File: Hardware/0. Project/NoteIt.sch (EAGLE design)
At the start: 61 parts, among them CN1 USB 3.2 Gen 2 Type C Receptac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, CN3 Micro-SD Card, CN4 FTSH-105-01-L-DV-K-TR, CN6 Lithium Ion Polymer, IC2 MCP73831/OT, IC5 S-8261ACMMD-G4MT2U, Q1 SI2374DS, Q2 SI2374DS, Q4 BC817-16LT1SMD, SW1 KY-040, U1 SN74AHC1G125DBV, U10 MSP430FR2476TPTR, U2 GL823K, U3 TLV75530PDBVR, U4 TS3A27518EPWR, U8 DS3231/SO, X2 CRYSTAL-MINI

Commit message: board design wip
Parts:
- removed CN2: (no value), con-ptr500:AK500/2-H
- added P1: OSTTE020104, Terminal Block 2P 3.5pitch:OSTTE020104
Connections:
- net 0V: now also P1.2; no longer CN2-2.KL
- net N$4: now also P1.1; no longer CN2-1.KL
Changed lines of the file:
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@@
 <setting verticaltext="up"/>
 </settings>
-<grid distance="0.025" unitdist="inch" unit="inch" style="lines" multiple="1" display="no" altdistance="0.01" altunitdist="inch" altunit="inch"/>
+<grid distance="0.1" unitdist="inch" unit="inch" style="lines" multiple="1" display="no" altdistance="0.01" altunitdist="inch" altunit="inch"/>
 <layers>
 <layer number="1" name="Top" color="4" fill="1" visible="no" active="no"/>
@@
 <part name="SUPPLY28" library="My-Supply" deviceset="0V" device=""/>
 <part name="SUPPLY29" library="My-Supply" deviceset="3.3V" device=""/>
-<part name="CN2" library="con-ptr500" deviceset="AK500/2-H" device="" package3d_urn="urn:adsk.eagle:package:9901/1" override_package3d_urn="urn:adsk.eagle:package:32815263/2" override_package_urn="urn:adsk.eagle:footprint:9865/1"/>
 <part name="SUPPLY32" library="My-Supply" deviceset="0V" device=""/>
 <part name="R1" library="My-RLC" deviceset="R_" device="0603" package3d_urn="urn:adsk.eagle:package:23494030/2"/>
@@
 <part name="SUPPLY12" library="My-Supply" deviceset="0V" device=""/>
 <part name="CN3" library="Micro SD" deviceset="MICROSD-PUSH-OUT" device="" package3d_urn="urn:adsk.eagle:package:32766245/3" value="Micro-SD Card"/>
-<part name="BAT1" library="SamacSys_Parts" deviceset="CR1220" device=""/>
+<part name="BAT1" library="SamacSys_Parts" deviceset="CR1220" device="" package3d_urn="urn:adsk.eagle:package:32858608/4"/>
 <part name="CN6" library="Battery" deviceset="BATTERY" device="JST-2" package3d_urn="urn:adsk.eagle:package:32835973/2" value="Lithium Ion Polymer"/>
 <part name="Q1" library="SI2374DS" deviceset="SI2374DS" device="SOT23" package3d_urn="urn:adsk.eagle:package:32844852/2" value="SI2374DS"/>
 <part name="Q2" library="SI2374DS" deviceset="SI2374DS" device="SOT23" package3d_urn="urn:adsk.eagle:package:32844852/2" value="SI2374DS"/>
 <part name="U3" library="TLV75530PDBVR" deviceset="TLV75530PDBVR" device="" package3d_urn="urn:adsk.eagle:package:32842001/2"/>
+<part name="P1" library="Terminal Block 2P 3.5pitch" deviceset="OSTTE020104" device="" override_package3d_urn="urn:adsk.eagle:package:32867978/2" override_package_urn="urn:adsk.eagle:footprint:32867979/1"/>
 </parts>
 <sheets>
@@
 <attribute name="VALUE" x="288.3154" y="76.2" size="1.778" layer="96" align="center"/>
 </instance>
-<instance part="CN2" gate="-1" x="273.685" y="57.15" smashed="yes" grouprefs="DATALOGGER_INPUT">
-<attribute name="NAME" x="272.415" y="58.039" size="1.778" layer="95" rot="R180"/>
-</instance>
-<instance part="CN2" gate="-2" x="273.685" y="43.18" smashed="yes" grouprefs="DATALOGGER_INPUT">
-<attribute name="NAME" x="272.415" y="44.069" size="1.778" layer="95" rot="R180"/>
-<attribute name="VALUE" x="269.875" y="39.497" size="1.778" layer="96"/>
-</instance>
 <instance part="SUPPLY32" gate="G$1" x="55.245" y="153.67" smashed="yes" grouprefs="MICRO_SDCARD_CONTROLLER"/>
 <instance part="R1" gate="G$1" x="55.245" y="191.77" smashed="yes" rot="R270" grouprefs="MICRO_SDCARD_CONTROLLER">
@@
 <attribute name="NAME" x="320.04" y="387.715" size="2.0828" layer="95" ratio="10" rot="SR0"/>
 <attribute name="VALUE" x="320.04" y="385.255" size="2.0828" layer="96" ratio="10" rot="SR0"/>
+</instance>
+<instance part="P1" gate="G$1" x="273.685" y="57.15" smashed="yes" rot="MR0" grouprefs="DATALOGGER_INPUT">
+<attribute name="NAME" x="273.685" y="59.69271875" size="1.271359375" layer="95" rot="MR0"/>
+<attribute name="VALUE" x="271.137209375" y="39.37" size="1.271559375" layer="96" rot="MR90"/>
 </instance>
 </instances>
@@
 <wire x1="288.29" y1="49.53" x2="288.29" y2="43.18" width="0.1524" layer="91" grouprefs="DATALOGGER_INPUT"/>
 <junction x="288.29" y="43.18" grouprefs="DATALOGGER_INPUT"/>
-<pinref part="CN2" gate="-2" pin="KL"/>
 <pinref part="SUPPLY28" gate="G$1" pin="0V"/>
 <wire x1="288.29" y1="38.735" x2="288.29" y2="43.18" width="0.1524" layer="91" grouprefs="DATALOGGER_INPUT"/>
+<pinref part="P1" gate="G$1" pin="2"/>
+<wire x1="278.765" y1="54.61" x2="278.765" y2="43.18" width="0.1524" layer="91"/>
 </segment>
 <segment>
@@
 <pinref part="U1" gate="G$1" pin="IN"/>
 <wire x1="278.765" y1="57.15" x2="280.67" y2="57.15" width="0.1524" layer="91" grouprefs="DATALOGGER_INPUT"/>
-<pinref part="CN2" gate="-1" pin="KL"/>
-</segment>
-</net>
+<pinref part="P1" gate="G$1" pin="1"/>
+</segment>
+</net>

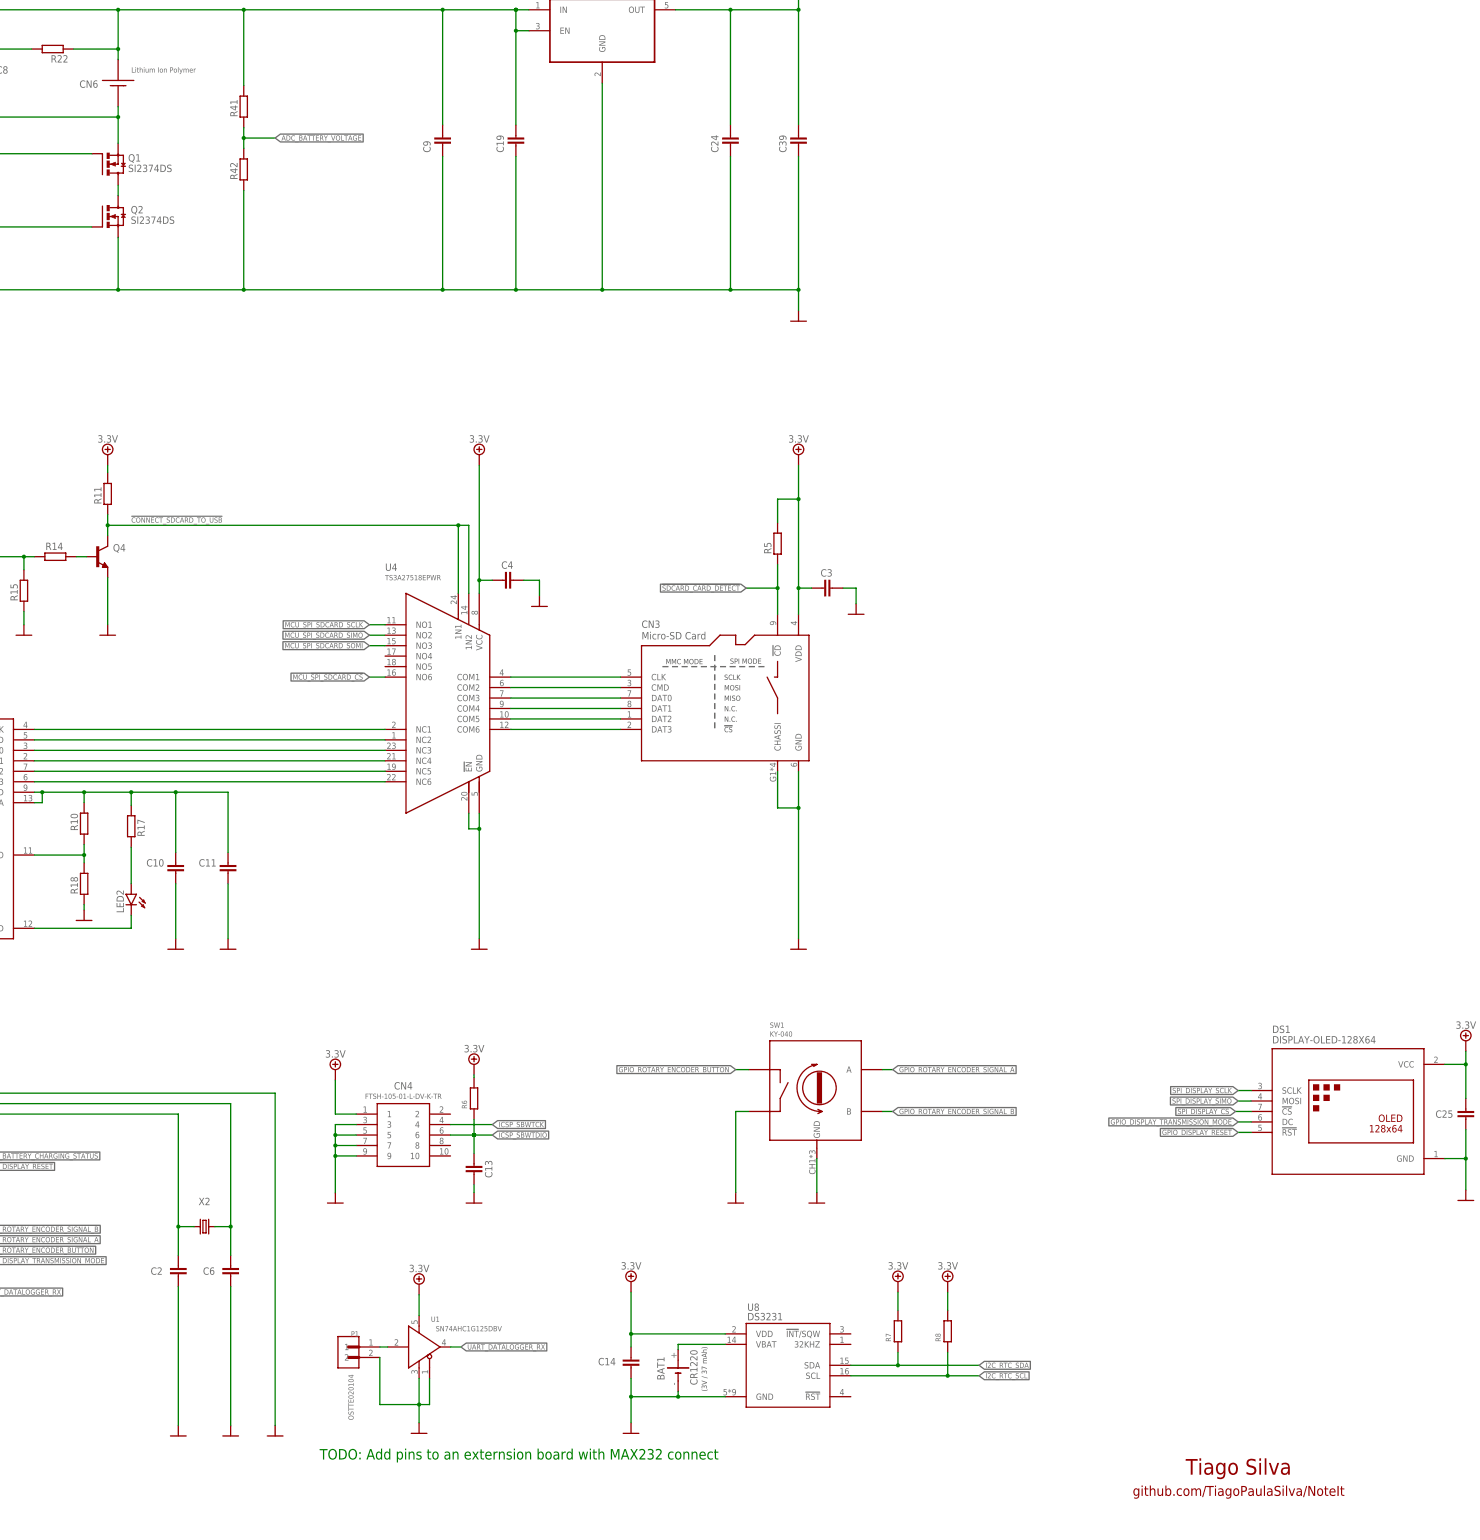
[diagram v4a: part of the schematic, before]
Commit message: Added external pull ups to rotary encoder
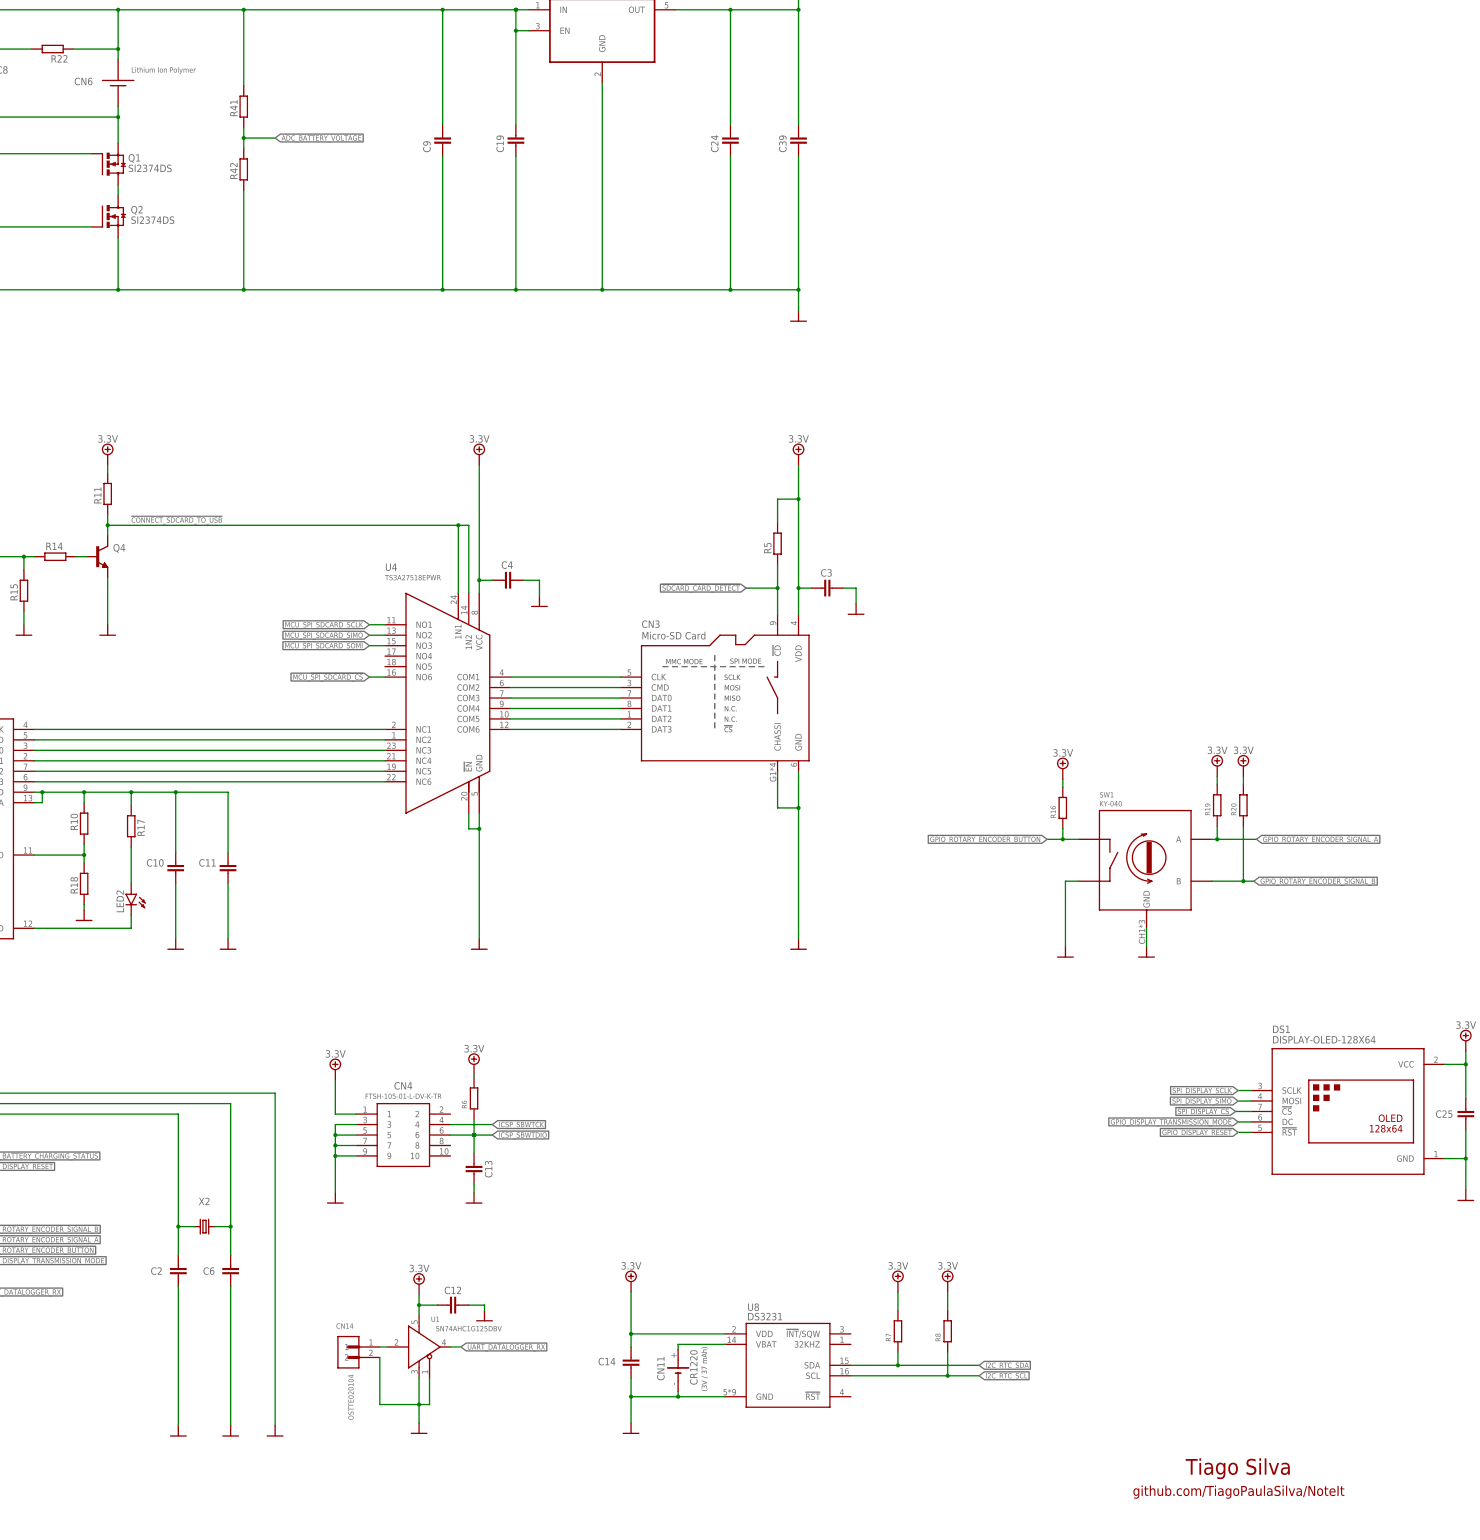
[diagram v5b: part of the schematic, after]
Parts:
- added C12: (no value), My-RLC:C_0603
- added R16, R19, R20: (no value), My-RLC:R_0603
- renumbered BAT1 to CN11, P1 to CN14
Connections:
- net 0V: now also C12.2
- net 3.3V: now also C12.1, R16.1, R19.1, R20.1
- net GPIO_ROTARY_ENCODER_BUTTON: now also R16.2
- net GPIO_ROTARY_ENCODER_SIGNAL_A: now also R19.2
- net GPIO_ROTARY_ENCODER_SIGNAL_B: now also R20.2
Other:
- note removed: "TODO: Add pins to an externsion board with MAX232 connect"
- moved on the sheet: SW1

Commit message: NoteIt v1.0 release
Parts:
- removed C25, C39: (no value), My-RLC:C_0603
- removed CN11: CR1220, SamacSys_Parts:CR1220
- removed CN14: OSTTE020104, Terminal Block 2P 3.5pitch:OSTTE020104
- removed IC2: MCP73831/OT, adafruit:MCP73831/OT
- removed IC5: S-8261ACMMD-G4MT2U, SamacSys_Parts:S-8261ACMMD-G4MT2U
- removed Q4: BC817-16LT1SMD, transistor-npn:BC817-16LT1SMD
- removed R41, R42: (no value), My-RLC:R_0603
- removed U10: MSP430FR2476TPTR, MSP430FR2476TPTR:MSP430FR2476TPTR
- removed X2: CRYSTAL-MINI, crystal-geyer_V1_0:CRYSTAL-MINI
- added C17, C20: 100nF, My-RLC:C_0603
- added CN2: Lithium Ion Polymer, Battery:BATTERYJST-2
- added CN5: CR1220, SamacSys_Parts:CR1220
- added Q3: SI2374DS, SI2374DS:SI2374DSSOT23
- added R21, R23: 10k (5%), My-RLC:R_0603
- added U5: SN74AHC1G125DBV, SN74AHC1G125DRLR:SN74AHC1G125DBV
- added U6: TS3A27518EPWR, TS3A27518EPWR:TS3A27518EPWR
- added U7: TLV75530PDBVR, TLV75530PDBVR:TLV75530PDBVR
- added Y1: 32.768 kHz, crystal-geyer_V1_0:CRYSTAL-MINI
- C1: value (none) -> 10uF x 10V; PN (none) -> GRM188R61A106ME69D
- C10: value (none) -> 10uF
- C11, C12, C15, C16, C19, C4, C7: value (none) -> 100nF
- C13: value (none) -> 1nF x 50V
- C14, C18: value (none) -> 1uF
- C2: value (none) -> 100nF; PN C0603C220J1GACTU -> C0603C104M5RACTU
- C21: value (none) -> 100nF; PN GRM188R61A106ME69D -> (none)
- C3: value (none) -> 4.7nF
- C5: value (none) -> 10uF; PN C0603C104M5RACTU -> (none)
- C6: value (none) -> 100nF; PN C0603C220J1GACTU -> (none)
- C8, C9: value (none) -> 22pF x 100V; PN (none) -> C0603C220J1GACTU
- CN3: value Micro-SD Card -> OSTTE020104; device Micro SD:MICROSD-PUSH-OUT -> Terminal Block 2P 3.5pitch:OSTTE020104
- CN6: value Lithium Ion Polymer -> Micro-SD Card; device Battery:BATTERYJST-2 -> Micro SD:MICROSD-PUSH-OUT
- Q1: value SI2374DS -> BC817; device SI2374DS:SI2374DSSOT23 -> transistor-npn:BC817-16LT1SMD
- R1, R15, R2, R4: value (none) -> 1M
- R10, R19, R20: value (none) -> 4K7 (5%)
- R11: value (none) -> 4k7
- R12: value (none) -> 10k
- R13, R18: value (none) -> 10k (5%)
- R14: value (none) -> 1k (5%)
- R16: value (none) -> 1M; PN RC0603JR-1047KL -> (none)
- R17: value (none) -> 47k (5%); PN (none) -> RC0603JR-1047KL
- R22: value (none) -> 10k (5%); PN (none) -> RC0603JR-1047KL
- R3: value (none) -> 5k1 (5%)
- R5: value (none) -> 4K7
- R6: value (none) -> 5k1 (5%); PN RC0603JR-1047KL -> (none)
- R7: value (none) -> 2k; PN RC0603JR-1047KL -> (none)
- R8: value (none) -> 10k (5%); PN RC0603JR-1047KL -> (none)
- R9: value (none) -> 470R
- U1: value SN74AHC1G125DBV -> MCP73831/2; device SN74AHC1G125DRLR:SN74AHC1G125DBV -> adafruit:MCP73831/OT
- U2: value GL823K -> MSP430FR2476TPTR; device SamacSys_Parts:GL823K -> MSP430FR2476TPTR:MSP430FR2476TPTR; PN (none) -> MSP430FR2476TPTR
- U3: value TLV75530PDBVR -> S-8261ACMMD-G4MT2U; device TLV75530PDBVR:TLV75530PDBVR -> SamacSys_Parts:S-8261ACMMD-G4MT2U
- U4: value TS3A27518EPWR -> GL823K; device TS3A27518EPWR:TS3A27518EPWR -> SamacSys_Parts:GL823K
- renumbered C24 to C18, LED2 to LED1
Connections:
- net !CONNECT_SDCARD_TO_USB: now also Q1.C, R13.1, U6.1N1, U6.1N2; no longer Q4.C, R11.1, U4.1N1, U4.1N2
- net !GPIO_DISPLAY_RESET: now also U2.P6.2/TB0.0; no longer U10.P6.2/TB0.0
- net !SDCARD_CARD_DETECT!: now also CN6.!CD, R18.2, U2.P4.6/UCB0SIMO/UCB0SDA/TA3.1; no longer CN3.!CD, R5.2, U10.P4.6/UCB0SIMO/UCB0SDA/TA3.1
- net !SPI_DISPLAY_CS: now also U2.P5.4/UCB1STE/TA3CLK/A11; no longer U10.P5.4/UCB1STE/TA3CLK/A11
- net 0V: now also C1.2, C14.2, C16.2, C17.1, C20.1, C5.1, C6.1, C8.2, CN3.2, CN5.-, CN6.CHASSI, CN6.GND, Q1.E, Q3.S, R16.1, R2.1, R4.2, R5.1, R6.2, R7.1, R8.2, U1.VSS, U2.DVSS, U4.VSS_1, U4.VSS_2, U5.!OE, U5.GND, U6.!EN, U6.GND, U7.GND; no longer C1.1, C14.1, C16.1, C25.2, C39.2, C5.2, C6.2, C7.1, CN11.-, CN14.2, CN3.CHASSI, CN3.GND, IC2.VSS, Q2.S, Q4.E, R1.2, R13.1, R15.2, R18.1, R2.2, R42.1, R9.1, U1.!OE, U1.GND, U10.DVSS, U2.VSS_1, U2.VSS_2, U3.GND, U4.!EN, U4.GND
- net 3.3V: now also C1.1, C15.2, C17.2, C19.1, C2.1, C20.2, CN6.VDD, R13.2, R17.1, R18.1, R21.1, R22.1, R23.1, U2.DVCC, U5.VDD, U6.VCC, U7.OUT; no longer C14.2, C25.1, C3.2, C39.1, C4.2, C5.1, CN3.VDD, R11.2, R16.1, R5.1, R6.1, R7.1, R8.1, U1.VDD, U10.DVCC, U3.OUT, U4.VCC
- net ADC_BATTERY_VOLTAGE: now also R15.1, R16.2, U2.P1.0/UCB0STE/TA0CLK/A0/VEREF+; no longer R41.1, R42.2, U10.P1.0/UCB0STE/TA0CLK/A0/VEREF+
- net GPIO_BATTERY_CHARGING_STATUS: now also U1.STAT, U2.P4.7/UCA0STE/TB0.1; no longer IC2.STAT, U10.P4.7/UCA0STE/TB0.1
- net GPIO_DISPLAY_TRANSMISSION_MODE: now also U2.P3.7/TA3.2; no longer U10.P3.7/TA3.2
- net GPIO_ROTARY_ENCODER_BUTTON: now also R21.2, U2.P4.0/TA3.1; no longer R16.2, U10.P4.0/TA3.1
- net GPIO_ROTARY_ENCODER_SIGNAL_A: now also R22.2, U2.P4.1/TA3.0; no longer R19.2, U10.P4.1/TA3.0
- net GPIO_ROTARY_ENCODER_SIGNAL_B: now also R23.2, U2.P4.2/TA3CLK; no longer R20.2, U10.P4.2/TA3CLK
- net GPIO_USB_DETECT: now also R1.1, R2.2, U2.P4.5/UCB0SOMI/UCB0SCL/TA3.2; no longer R4.1, R9.2, U10.P4.5/UCB0SOMI/UCB0SCL/TA3.2
- net I2C_RTC_SCL: now also R20.2, U2.P1.3/UCB0SOMI/UCB0SCL/MCLK/A3; no longer R8.2, U10.P1.3/UCB0SOMI/UCB0SCL/MCLK/A3
- net I2C_RTC_SDA: now also R19.2, U2.P1.2/UCB0SIMO/UCB0SDA/TA0.2/A2/VEREF-; no longer R7.2, U10.P1.2/UCB0SIMO/UCB0SDA/TA0.2/A2/VEREF-
- net ICSP_SBWTCK: now also U2.TEST/SBWTCK; no longer U10.TEST/SBWTCK
- net ICSP_SBWTDIO: now also R17.2, U2.!RST!/NMI/SBWTDIO; no longer R6.2, U10.!RST!/NMI/SBWTDIO
- net MCU_!SPI_SDCARD_CS: now also U2.P1.7/UCA0STE/SMCLK/TDO/A7, U6.NO6; no longer U10.P1.7/UCA0STE/SMCLK/TDO/A7, U4.NO6
- net MCU_SPI_SDCARD_SCLK: now also U2.P1.6/UCA0CLK/TA1CLK/TDI/TCLK/A6, U6.NO1; no longer U10.P1.6/UCA0CLK/TA1CLK/TDI/TCLK/A6, U4.NO1
- net MCU_SPI_SDCARD_SIMO: now also U2.P1.4/UCA0TXD/UCA0SIMO/TA1.2/TCK/A4/VREF+, U6.NO2; no longer U10.P1.4/UCA0TXD/UCA0SIMO/TA1.2/TCK/A4/VREF+, U4.NO2
- net MCU_SPI_SDCARD_SOMI: now also U2.P1.5/UCA0RXD/UCA0SOMI/TA1.1/TMS/A5, U6.NO3; no longer U10.P1.5/UCA0RXD/UCA0SOMI/TA1.1/TMS/A5, U4.NO3
- net N$1: now also Q2.G, U3.DO; no longer IC5.DO, Q1.G
- net N$10: now also C3.2, R4.1; no longer C1.2, R3.1
- net N$11: now also R11.1, R14.1, U4.VDD, U4.VDDA; no longer R10.1, R17.1, U2.VDD, U2.VDDA
- net N$12: now also R11.2, R12.2, U4.GPIO; no longer R10.2, R18.2, U2.GPIO
- net N$13: now also C6.2, U4.PMOS; no longer C15.2, U2.PMOS
- net N$14: now also Q1.B, R10.1; no longer Q4.B, R14.1
- net N$15: now also CN6.CMD, U6.COM2; no longer CN3.CMD, U4.COM2
- net N$16: now also CN6.DAT0, U6.COM3; no longer CN3.DAT0, U4.COM3
- net N$2: now also CN6.CLK, U6.COM1; no longer CN3.CLK, U4.COM1
- net N$20: now also CN6.DAT1, U6.COM4; no longer CN3.DAT1, U4.COM4
- net N$21: now also R6.1; no longer R2.1
- net N$22: now also CN5.+; no longer CN11.+
- net N$26: now also R5.2, U1.PROG; no longer IC2.PROG, R12.2
- net N$27: now also Q3.G, U3.CO; no longer IC5.CO, Q2.G
- net N$29: now also R7.2, U3.VM; no longer IC5.VM, R13.2
- net N$3: now also Q3.D; no longer Q1.D
- net N$31: now also C7.1, R9.2, U3.VDD; no longer C8.1, IC5.VDD, R22.2
- net N$32: now also C7.2, CN2.GND, Q2.S, U3.VSS; no longer C8.2, CN6.GND, IC5.VSS, Q1.S
- net N$33: now also C14.1, C16.1, CN2.VDD, R15.2, R9.1, U1.VBAT, U7.EN, U7.IN; no longer C19.1, C9.1, CN6.VDD, IC2.VBAT, R22.1, R41.2, U3.EN, U3.IN
- net N$4: now also CN3.1, U5.IN; no longer CN14.1, U1.IN
- net N$5: now also U4.LED; no longer U2.LED
- net N$6: now also R3.1; no longer R1.1
- net N$7: now also CN6.DAT2, U6.COM5; no longer CN3.DAT2, U4.COM5
- net N$8: now also CN6.DAT3, U6.COM6; no longer CN3.DAT3, U4.COM6
- net N$9: now also R14.2; no longer R17.2
- net SPI_DISPLAY_SCLK: now also U2.P5.3/UCB1CLK/TA3.0/A10; no longer U10.P5.3/UCB1CLK/TA3.0/A10
- net SPI_DISPLAY_SIMO: now also U2.P4.4/UCB1SIMO/UCB1SDA/TB0.6/A9; no longer U10.P4.4/UCB1SIMO/UCB1SDA/TB0.6/A9
- net UART_DATALOGGER_RX: now also U2.P2.5/UCA1RXD/UCA1SOMI, U5.OUT; no longer U1.OUT, U10.P2.5/UCA1RXD/UCA1SOMI
- net USB_CLK: now also U4.CLK, U6.NC1; no longer U2.CLK, U4.NC1
- net USB_CMD: now also U4.CMD, U6.NC2; no longer U2.CMD, U4.NC2
- net USB_DAT0: now also U4.DAT0, U6.NC3; no longer U2.DAT0, U4.NC3
- net USB_DAT1: now also U4.DAT1, U6.NC4; no longer U2.DAT1, U4.NC4
- net USB_DAT2: now also U4.DAT2, U6.NC5; no longer U2.DAT2, U4.NC5
- net USB_DAT3: now also U4.DAT3, U6.NC6; no longer U2.DAT3, U4.NC6
- net USB_N: now also U4.DP; no longer U2.DP
- net USB_P: now also U4.DN; no longer U2.DN
- net VUSB: now also C4.2, C5.2, R1.2, R10.2, R8.1, U1.VDD, U4.5V; no longer C16.2, C7.2, IC2.VDD, R14.2, R15.1, R4.2, U2.5V
- net XTAL_IN: now also C8.1, U2.P2.0/XOUT, Y1.1; no longer C2.1, U10.P2.0/XOUT, X2.1
- net XTAL_OUT: now also C9.1, U2.P2.1/XIN, Y1.2; no longer C6.1, U10.P2.1/XIN, X2.2
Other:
- moved on the sheet: C1, C12, C13, C14, C15, C16, C19, C2, C21, C3, C4, C5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

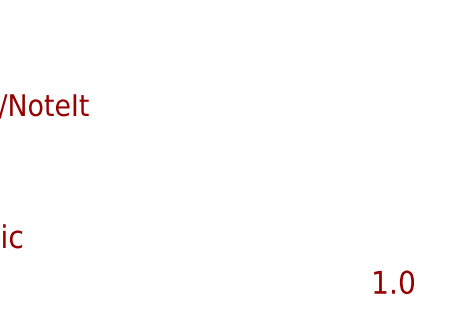
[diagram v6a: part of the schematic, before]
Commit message: NoteIt v1.1 release (details in commit description)
- Vias with 0.2mm and 0.4mm diameter drill changed to 0.3mm and 0.6mm diameter drill.
- The first approach makes the production of PCBs much more expensive (JLCPCB experience).
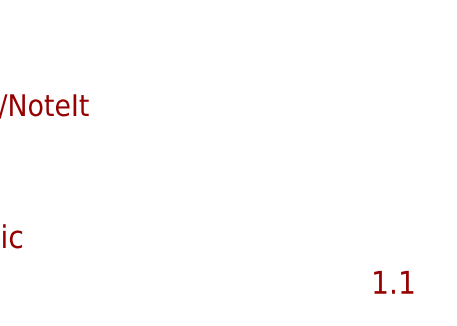
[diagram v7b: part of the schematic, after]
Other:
- note added: "1.1"
- note removed: "1.0"
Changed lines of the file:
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@@
 <setting verticaltext="up"/>
 </settings>
-<grid distance="0.025" unitdist="inch" unit="inch" style="lines" multiple="1" display="no" altdistance="0.01" altunitdist="inch" altunit="inch"/>
+<grid distance="0.1" unitdist="inch" unit="inch" style="lines" multiple="1" display="no" altdistance="0.01" altunitdist="inch" altunit="inch"/>
 <layers>
 <layer number="1" name="Top" color="4" fill="1" visible="no" active="no"/>
@@
 <text x="487.172" y="28.067" size="3.81" layer="94" align="center">Tiago Silva</text>
 <text x="487.172" y="22.225" size="2.413" layer="94" align="center">github.com/TiagoPaulaSilva/NoteIt</text>
-<text x="544.195" y="1.27" size="2.54" layer="94" ratio="5">1.0</text>
+<text x="544.195" y="1.27" size="2.54" layer="94" ratio="5">1.1</text>
 <text x="473.075" y="6.35" size="2.54" layer="94" ratio="5">Complete Schematic</text>
 <text x="437.515" y="183.515" size="1.27" layer="98" align="center" grouprefs="ROTARY_ENCODER">needs MCU pull-up</text>
